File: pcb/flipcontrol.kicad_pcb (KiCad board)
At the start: 2 copper layers, 59.7 x 132.8 mm, 33 parts, among them J1 PROGRAMMING, J2 SERIAL_IN, J3 18V_POWER_IN, J4 LED_STRIP, J5 DOT_BOARD, Q1 FQP27P06, Q2 2N3904BU, Q3 FQP27P06, Q4 2N3904BU, U1 LM2576HVT-5, U2 LM1085-3.3

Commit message: Update for Kicad 7, update some components
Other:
- net class 4A trace removed
- net class Default removed

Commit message: Update PCB
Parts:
- removed J1: PROGRAMMING, Connector_PinHeader_2.54mm:PinHeader_1x04_P2.54mm_Vertical
- removed the J2 at (142.0, 80.8)
- removed MOD1: ESP32-WROOM-32, digikey-footprints:ESP32-WROOM-32D
- removed the R3 at (105.0, 68.1)
- removed the R5 at (109.8, 158.8)
- removed S2: RESET, pushbutton:1825910-6
- added C6: 100nF, Capacitor_SMD:C_0805_2012Metric, F.Cu at (21.4, 83.6)
- added C7: 10uF, Capacitor_SMD:C_0805_2012Metric, F.Cu at (21.4, 86.6)
- added C8: 100nF, Capacitor_SMD:C_0805_2012Metric, F.Cu at (21.4, 89.6)
- added C9: 10uF, Capacitor_SMD:C_0805_2012Metric, F.Cu at (21.4, 92.6)
- added D3: D, Diode_SMD:D_SOD-123, F.Cu at (11.7, 93.3)
- added D4: D, Diode_SMD:D_SOD-123, F.Cu at (11.7, 96.7)
- added F1: Polyfuse, Fuse:Fuse_1206_3216Metric, F.Cu at (26.4, 97.6)
- added J5: DOT_BOARD_3, Connector_IDC:IDC-Header_2x07_P2.54mm_Vertical, F.Cu at (96.6, 129.4)
- added Q5: MMBT3904, Package_TO_SOT_SMD:SOT-23, F.Cu at (206.1, 85.9)
- added R1: 10K, Resistor_SMD:R_0805_2012Metric, F.Cu at (16.9, 80.5)
- added R10: 5.1K, Resistor_SMD:R_0805_2012Metric, F.Cu at (16.9, 98.2)
- added R4: 2K, Resistor_SMD:R_0805_2012Metric, F.Cu at (16.9, 83.5)
- added R8: 10K, Resistor_SMD:R_0805_2012Metric, F.Cu at (210.6, 69.2)
- added R9: 5.1K, Resistor_SMD:R_0805_2012Metric, F.Cu at (16.9, 95.3)
- added U3: ESP32-S3-WROOM-1, Espressif:ESP32-S3-WROOM-1, F.Cu at (126.2, 111.0)
- added U4: CH340C, Package_SO:SOIC-16_3.9x9.9mm_P1.27mm, F.Cu at (143.6, 105.4)
- C1: value 0.1uF -> 100nF; footprint Capacitor_THT:C_Disc_D3.0mm_W1.6mm_P2.50mm -> Capacitor_SMD:C_0805_2012Metric
- C2: footprint Capacitor_THT:CP_Radial_D5.0mm_P2.50mm -> Capacitor_SMD:CP_Elec_10x10
- C3, C4: footprint Capacitor_THT:CP_Radial_D5.0mm_P2.50mm -> Capacitor_SMD:C_0805_2012Metric
- C5: value 330uF -> 220uF; footprint Capacitor_THT:CP_Radial_D5.0mm_P2.50mm -> Capacitor_SMD:CP_Elec_10x10
- D1: footprint Diode_THT:D_DO-15_P10.16mm_Horizontal -> Diode_SMD:D_SMB
- D2: value D_Schottky -> ESP_LED; footprint Diode_THT:D_DO-15_P10.16mm_Horizontal -> LED_SMD:LED_0805_2012Metric
- J2: renamed from J5; value DOT_BOARD -> DOT_BOARD_1
- J3: value 18V_POWER_IN -> DOT_BOARD_2; footprint Connector_Wire:SolderWirePad_1x02_P5.08mm_Drill1.5mm -> Connector_IDC:IDC-Header_2x07_P2.54mm_Vertical
- L1: value 220uH -> 33uH; footprint Inductor_THT:L_Radial_D8.7mm_P5.00mm_Fastron_07HCP -> Inductor_SMD:L_12x12mm_H6mm
- Q1: value FQP27P06 -> UMH3N; footprint digikey-footprints:TO-220-3 -> SamacSys_Parts:SOT65P230X110-6N
- Q2, Q4: value 2N3904BU -> AO4419; footprint digikey-footprints:TO-92-3 -> SamacSys_Parts:SOIC127P600X175-8N
- Q3: value FQP27P06 -> MMBT3904; footprint digikey-footprints:TO-220-3 -> Package_TO_SOT_SMD:SOT-23
- R2: renamed from R1; footprint Resistor_THT:R_Axial_DIN0204_L3.6mm_D1.6mm_P5.08mm_Horizontal -> Resistor_SMD:R_0805_2012Metric
- R3: renamed from R2; footprint Resistor_THT:R_Axial_DIN0204_L3.6mm_D1.6mm_P5.08mm_Horizontal -> Resistor_SMD:R_0805_2012Metric
- R5: renamed from R4; footprint Resistor_THT:R_Axial_DIN0204_L3.6mm_D1.6mm_P5.08mm_Horizontal -> Resistor_SMD:R_0805_2012Metric
- R6: value 10K -> 100R; footprint Resistor_THT:R_Axial_DIN0204_L3.6mm_D1.6mm_P5.08mm_Horizontal -> Resistor_SMD:R_0805_2012Metric
- R7: footprint Resistor_THT:R_Axial_DIN0204_L3.6mm_D1.6mm_P5.08mm_Horizontal -> Resistor_SMD:R_0805_2012Metric
- S1: value PROGRAM -> RESET; footprint pushbutton:1825910-6 -> SamacSys_Parts:FSM2JRT
- U1: value LM2576HVT-5 -> LM2596S-5; footprint Package_TO_SOT_THT:TO-220-5_Vertical -> Package_TO_SOT_SMD:TO-263-5_TabPin3
- U2: value LM1085-3.3 -> AMS1117-3.3; footprint digikey-footprints:TO-220-3 -> Package_TO_SOT_SMD:SOT-223-3_TabPin2
- moved R7 119.3 mm to (199.2, 79.5)
- moved R6 112.7 mm to (194.3, 66.0)
- moved D1 112.4 mm to (220.1, 157.9)
- moved D2 104.3 mm to (21.4, 95.6)
- moved Q4 102.9 mm to (184.4, 78.1), turned to 0 degrees
- moved C1 94.4 mm to (21.4, 80.6), turned to 0 degrees
- moved J4 93.5 mm to (188.2, 91.0)
- moved S1 89.1 mm to (36.7, 98.0)
- moved C5 82.0 mm to (224.1, 141.2)
- moved Q1 80.5 mm to (26.3, 106.6), turned to 0 degrees
- moved R5 78.8 mm to (183.4, 135.6)
- moved L1 78.4 mm to (196.9, 142.6)
- moved U1 78.1 mm to (165.5, 170.0), turned to 0 degrees
- moved C2 73.3 mm to (178.7, 154.6)
- moved J3 69.2 mm to (96.3, 99.9), turned to 0 degrees
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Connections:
- C1 pad 1: GND -> EN
- C1 pad 2: +3V3 -> GND
- D2 pad 1: +24V -> GND
- D2 pad 2: Net-(D2-Pad2) -> Net-(D2-A)
- J2 pad 10: ROW_ADVANCE -> ROW_ADVANCE_1
- J2 pad 13: Net-(J5-Pad13) -> COIL_DRIVE_OUT
- J2 pad 14: +24V -> COIL_DRIVE_OUT
- J2 pad 6: Net-(J5-Pad6) -> GND
- J2 pad 7: COL_ADVANCE -> COL_ADVANCE_1
- J2 pad 8: RESET -> RESET_1
- J2 pad 9: SET_UNSET -> SET_UNSET_1
- J3 pad 1: Net-(D2-Pad2) -> GND
- J3 pad 2: GND -> ENABLE_1
- Q1 pad 1: Net-(Q1-Pad1) -> RTS
- Q1 pad 2: COIL_DRIVE_OUT -> DTR
- Q1 pad 3: +24V -> IO0
- Q2 pad 1: GND -> +24V
- Q2 pad 2: Net-(Q2-Pad2) -> +24V
- Q2 pad 3: Net-(Q2-Pad3) -> +24V
- Q3 pad 1: Net-(Q3-Pad1) -> Net-(Q3-B)
- Q3 pad 2: LED_OUT -> GND
- Q3 pad 3: +24V -> Net-(Q3-C)
- Q4 pad 1: GND -> +24V
- Q4 pad 2: Net-(Q4-Pad2) -> +24V
- Q4 pad 3: Net-(Q4-Pad3) -> +24V
- R2 pad 1: Net-(Q2-Pad3) -> Net-(Q3-C)
- R2 pad 2: Net-(Q1-Pad1) -> Net-(Q2-G)
- R3 pad 1: Net-(Q2-Pad2) -> Net-(Q3-B)
- R5 pad 2: Net-(Q2-Pad3) -> Net-(Q3-C)
- R6 pad 1: Net-(Q4-Pad2) -> Net-(Q5-C)
- R6 pad 2: LED_IN -> Net-(Q4-G)
- R7 pad 1: +24V -> Net-(Q5-B)
- R7 pad 2: Net-(Q4-Pad3) -> LED_IN
- S1 pad 2: Net-(S1-Pad2) -> EN
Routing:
- net +5V: track 159.7 -> 0.00 mm, vias 2 -> 0
- net +24V: track 131.8 -> 0.00 mm, vias 4 -> 0
- net +3V3: track 102.9 -> 0.00 mm
- net LED_IN: track 88.2 -> 0.00 mm, vias 4 -> 0
- net COIL_DRIVE_IN: track 71.7 -> 0.00 mm, vias 2 -> 0
- net Net-(MOD1-Pad3): track 69.8 -> 0.00 mm
- net LED_OUT: track 59.1 -> 0.00 mm
- net SET_UNSET: track 53.1 -> 0.00 mm, vias 2 -> 0
- net ROW_ADVANCE: track 49.6 -> 0.00 mm, vias 2 -> 0
- net ENABLE_2: track 47.4 -> 0.00 mm
- net COL_ADVANCE: track 45.3 -> 0.00 mm, vias 2 -> 0
- net ENABLE_4: track 44.2 -> 0.00 mm
- net RESET: track 41.2 -> 0.00 mm, vias 2 -> 0
- net ENABLE_3: track 40.8 -> 0.00 mm
- net ENABLE_1: track 36.2 -> 0.00 mm
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- removed copper zone on F.Cu, net GND
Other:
- board text added: "Will Furnell 2023"
- board text added: "r2"
- board text removed: "+"
- board text removed: "-"
- board text removed: "18V IN"
- board text removed: "Note: This board has 18V, 5V and 3.3V rails!"
- board text removed: "PROGRAM"
- board text removed: "Will Furnell 2019"
- board text removed: "r1"
- board text removed: "will was here"

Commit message: Update with latest schematic and board changes
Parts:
- Q2, Q4: value AO4419 -> Si2347DS-T1-GE3; footprint SamacSys_Parts:SOIC127P600X175-8N -> SamacSys_Parts:SOT95P237X112-3N
- moved J4 106.9 mm to (117.5, 171.1), turned to 90 degrees
- moved L1 75.7 mm to (121.6, 150.1), turned to 180 degrees
- moved S1 63.8 mm to (80.5, 51.6)
- moved U3 57.0 mm to (120.3, 54.3)
- moved U1 31.6 mm to (141.0, 150.1)
- moved D2 29.8 mm to (51.2, 97.3)
- moved R1 29.8 mm to (46.7, 82.2)
- moved R10 29.8 mm to (46.7, 99.9)
- moved R4 29.8 mm to (46.7, 85.1)
- moved R9 29.8 mm to (46.7, 96.9)
- moved C1 29.8 mm to (51.2, 82.2)
- moved C6 29.8 mm to (51.2, 85.2)
- moved C7 29.8 mm to (51.2, 88.2)
- moved C8 29.8 mm to (51.2, 91.3)
- moved D3 29.8 mm to (41.5, 95.0)
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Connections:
- Q2 pad 1: +24V -> Net-(Q2-G)
- Q2 pad 3: +24V -> COIL_DRIVE_OUT
- Q4 pad 1: +24V -> Net-(Q4-G)
- Q4 pad 3: +24V -> LED_OUT
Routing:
- net COIL_DRIVE_OUT: track 86.7 -> 0.00 mm

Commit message: PCB layout
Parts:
- removed Q1: UMH3N, SamacSys_Parts:SOT65P230X110-6N
- added C10: 6.8nF, Capacitor_SMD:C_0805_2012Metric, F.Cu at (112.5, 90.4)
- added C11: 6.8nF, Capacitor_SMD:C_0805_2012Metric, F.Cu at (112.5, 93.0)
- added C12: 22nF, Capacitor_SMD:C_0805_2012Metric, F.Cu at (111.6, 108.5)
- added C13: 10nF, Capacitor_SMD:C_0805_2012Metric, F.Cu at (104.4, 82.5)
- added C14: 10nF, Capacitor_SMD:C_0805_2012Metric, F.Cu at (135.6, 97.1)
- added C15: 4.7uF, Capacitor_SMD:C_0805_2012Metric, F.Cu at (131.1, 100.4)
- added C16: 0.1uF, Capacitor_SMD:C_0805_2012Metric, F.Cu at (133.7, 100.4)
- added C17: 0.1uF, Capacitor_SMD:C_0805_2012Metric, F.Cu at (128.6, 100.4)
- added C18: 0.1uF, Capacitor_SMD:C_0805_2012Metric, F.Cu at (126.0, 100.4)
- added C19: 0.1uF, Capacitor_SMD:C_0805_2012Metric, F.Cu at (121.2, 89.4)
- added C20: 0.1uF, Capacitor_SMD:C_0805_2012Metric, F.Cu at (122.2, 93.7)
- added C21: 0.1uF, Capacitor_SMD:C_0805_2012Metric, F.Cu at (122.2, 95.8)
- added C22: 10uF/16V, Capacitor_SMD:C_0805_2012Metric, F.Cu at (137.5, 100.6)
- added C23: 10uF/16v, Capacitor_SMD:C_0805_2012Metric, F.Cu at (128.7, 84.7)
- added C24: 0.1uF, Capacitor_SMD:C_0805_2012Metric, F.Cu at (132.1, 84.7)
- added C25: 18pF, Capacitor_SMD:C_0805_2012Metric, F.Cu at (142.0, 88.2)
- added C26: 18pF, Capacitor_SMD:C_0805_2012Metric, F.Cu at (146.0, 94.5)
- added C27: 47 pF, Capacitor_SMD:C_0805_2012Metric, F.Cu at (193.6, 104.5)
- added C28: 47uF 3mΩ 16V, Capacitor_SMD:C_1210_3225Metric, F.Cu at (180.8, 92.4)
- added D5: 3V3, LED_SMD:LED_0805_2012Metric, F.Cu at (156.8, 106.3)
- added J1: PJ-202A, digikey-footprints:Barrel_Jack_5.5mmODx2.1mmID_PJ-202A, F.Cu at (208.2, 88.7)
- added J6: RJMG163118101NR, SamacSys_Parts:RJMG163118101NR, F.Cu at (104.5, 100.3)
- added J7: FTDI, Connector_PinHeader_2.54mm:PinHeader_1x06_P2.54mm_Vertical, F.Cu at (116.9, 118.6)
- added JP1: Bootloader, digikey-footprints:Jumper_Tin_P5.32mm, F.Cu at (126.2, 111.8)
- added L2: HH-1M1608-121JT, Inductor_SMD:L_0805_2012Metric, F.Cu at (141.1, 99.6)
- added R11: 33R, Resistor_SMD:R_0805_2012Metric, F.Cu at (116.9, 90.4)
- added R12: 33R, Resistor_SMD:R_0805_2012Metric, F.Cu at (116.9, 93.0)
- added R13: 33R, Resistor_SMD:R_0805_2012Metric, F.Cu at (112.5, 100.1)
- added R14: 33R, Resistor_SMD:R_0805_2012Metric, F.Cu at (112.5, 96.9)
- added R15: 49R9, Resistor_SMD:R_0805_2012Metric, F.Cu at (112.3, 104.1)
- added R16: 49R9, Resistor_SMD:R_0805_2012Metric, F.Cu at (115.9, 104.1)
- added R17: 10R, Resistor_SMD:R_0805_2012Metric, F.Cu at (104.7, 108.2)
- added R18: 49R9, Resistor_SMD:R_0805_2012Metric, F.Cu at (114.6, 86.1)
- added R19: 49R9, Resistor_SMD:R_0805_2012Metric, F.Cu at (117.1, 86.1)
- added R20: 12.4k 1%, Resistor_SMD:R_0805_2012Metric, F.Cu at (123.5, 100.3)
- added R21: 330R, Resistor_SMD:R_0805_2012Metric, F.Cu at (99.6, 108.0)
- added R22: 330R, Resistor_SMD:R_0805_2012Metric, F.Cu at (99.1, 82.5)
- added R23: 1M, Resistor_SMD:R_0805_2012Metric, F.Cu at (136.4, 92.7)
- added R25: 0.015 R, Resistor_SMD:R_0805_2012Metric, F.Cu at (157.9, 81.5)
- added R26: 10K, Resistor_SMD:R_0805_2012Metric, F.Cu at (127.8, 109.0)
- added R27: 52.3k, Resistor_SMD:R_0805_2012Metric, F.Cu at (196.1, 104.5)
- added R28: 10k, Resistor_SMD:R_0805_2012Metric, F.Cu at (198.7, 104.5)
- added R29: R_Small, Resistor_SMD:R_0805_2012Metric, F.Cu at (160.6, 101.6)
- added R30: R_Small, Resistor_SMD:R_0805_2012Metric, F.Cu at (156.8, 101.6)
- added TP1: Drive sense, TestPoint:TestPoint_Pad_D2.0mm, F.Cu at (141.0, 79.5)
- added TP2: Drive in, TestPoint:TestPoint_Pad_D2.0mm, F.Cu at (151.4, 90.7)
- added TP3: LED in, TestPoint:TestPoint_Pad_D2.0mm, F.Cu at (165.4, 87.1)
- added TP4: CS, TestPoint:TestPoint_Pad_D2.0mm, F.Cu at (128.1, 123.4)
- added TP5: SCLK, TestPoint:TestPoint_Pad_D2.0mm, F.Cu at (116.6, 123.4)
- added TP6: MISO, TestPoint:TestPoint_Pad_D2.0mm, F.Cu at (124.3, 123.4)
- added TP7: MOSI, TestPoint:TestPoint_Pad_D2.0mm, F.Cu at (120.4, 123.4)
- added U5: W5500, Package_QFP:LQFP-48_7x7mm_P0.5mm, F.Cu at (129.6, 92.6)
- added USB1: HRO-TYPE-C-31-M-12, Connector_USB:USB_C_Receptacle_HRO_TYPE-C-31-M-12, F.Cu at (174.6, 123.4)
- added Y1: Crystal_GND24, Crystal:Crystal_SMD_Abracon_ABM8G-4Pin_3.2x2.5mm, F.Cu at (142.4, 92.4)
- C2: value 100uF -> 10uF 2.8mΩ 35V; footprint Capacitor_SMD:CP_Elec_10x10 -> Capacitor_SMD:C_0805_2012Metric
- C5: value 220uF -> 100nF 30mΩ 50V; footprint Capacitor_SMD:CP_Elec_10x10 -> Capacitor_SMD:C_0805_2012Metric
- C9: value 10uF -> 100 nF 1mΩ 10V
- D1: value D_Schottky -> 5V; footprint Diode_SMD:D_SMB -> LED_SMD:LED_0805_2012Metric
- L1: value 33uH -> IHLP4040DZER6R8M01; footprint Inductor_SMD:L_12x12mm_H6mm -> Inductor_SMD:L_Vishay_IHLP-4040
- U1: value LM2596S-5 -> TPS563300; footprint Package_TO_SOT_SMD:TO-263-5_TabPin3 -> Package_TO_SOT_SMD:SOT-583-8
- U4: value CH340C -> NCS214; footprint Package_SO:SOIC-16_3.9x9.9mm_P1.27mm -> Package_TO_SOT_SMD:SOT-363_SC-70-6_Handsoldering
- moved D3 160.3 mm to (201.7, 91.3), turned to 90 degrees
- moved C9 145.8 mm to (196.8, 101.6)
- moved D4 140.3 mm to (181.5, 106.0), turned to -90 degrees
- moved R10 130.3 mm to (176.3, 113.6), turned to -90 degrees
- moved R9 126.4 mm to (172.0, 113.6), turned to -90 degrees
- moved F1 125.5 mm to (180.9, 113.0), turned to 90 degrees
- moved J4 117.2 mm to (193.4, 81.8), turned to -90 degrees
- moved R1 114.0 mm to (154.4, 119.6), turned to 180 degrees
- moved H2 111.9 mm to (209.4, 75.4), turned to -90 degrees
- moved S1 110.0 mm to (163.9, 123.4)
- moved C6 109.6 mm to (154.4, 122.2), turned to 180 degrees
- moved C7 109.5 mm to (154.4, 124.7)
- moved C1 108.9 mm to (154.4, 117.1)
- moved C8 96.7 mm to (147.4, 82.1), turned to 180 degrees
- moved H1 93.4 mm to (209.7, 115.6), turned to -90 degrees
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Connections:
- C2 pad 1: +24V -> +18V
- C5 pad 1: +5V -> +18V
- C9 pad 1: GND -> Net-(U1-SW)
- C9 pad 2: +3V3 -> Net-(U1-VBST)
- D1 pad 1: Net-(D1-K) -> GND
- D1 pad 2: GND -> Net-(D1-A)
- D3 pad 1: +24V -> +18V
- F1 pad 1: Net-(D4-A) -> USB_VBUS
- F1 pad 2: Net-(F1-Pad2) -> Net-(D4-A)
- L1 pad 1: Net-(D1-K) -> Net-(U1-SW)
- Q2 pad 2: +24V -> +18V
- Q2 pad 3: COIL_DRIVE_OUT -> Net-(Q2-D)
- Q4 pad 2: +24V -> +18V
- R5 pad 1: +24V -> +18V
- R8 pad 1: +24V -> +18V
- U1 pad 1: +24V -> unconnected-(U1-NC-Pad1)
- U1 pad 2: Net-(D1-K) -> unconnected-(U1-EN-Pad2)
- U1 pad 3: GND -> +18V
- U1 pad 4: +5V -> GND
- U1 pad 5: GND -> Net-(U1-SW)
- U3 pad 10: ROW_ADVANCE_2 -> SET_UNSET_2
- U3 pad 11: COL_ADVANCE_2 -> ROW_ADVANCE_2
- U3 pad 12: COL_ADVANCE_1 -> COL_ADVANCE_2
- U3 pad 13: unconnected-(U3-GPIO19/U1RTS/ADC2_CH8/CLK_OUT2/USB_D--Pad13) -> USB_DN
- U3 pad 14: unconnected-(U3-GPIO20/U1CTS/ADC2_CH9/CLK_OUT1/USB_D+-Pad14) -> USB_DP
- U3 pad 15: unconnected-(U3-GPIO3/TOUCH3/ADC1_CH2-Pad15) -> COIL_DRIVE_SENSE
- U3 pad 16: COL_ADVANCE_3 -> unconnected-(U3-GPIO46-Pad16)
- U3 pad 17: RESET_1 -> RESET_2
- U3 pad 22: SET_UNSET_2 -> RESET_3
- U3 pad 23: RESET_2 -> COL_ADVANCE_3
- U3 pad 24: RESET_3 -> ROW_ADVANCE_3
- U3 pad 25: ESP_LED -> SET_UNSET_3
- U3 pad 26: ROW_ADVANCE_3 -> unconnected-(U3-GPIO45-Pad26)
- U3 pad 28: unconnected-(U3-SPIIO6/GPIO35/FSPID/SUBSPID-Pad28) -> MOSI
- U3 pad 29: unconnected-(U3-SPIIO7/GPIO36/FSPICLK/SUBSPICLK-Pad29) -> SCLK
- U3 pad 30: unconnected-(U3-SPIDQS/GPIO37/FSPIQ/SUBSPIQ-Pad30) -> MISO
- U3 pad 31: SET_UNSET_3 -> ESP_LED
- U3 pad 34: unconnected-(U3-MTDI/GPIO41/CLK_OUT1-Pad34) -> ETH_RST
- U3 pad 35: unconnected-(U3-MTMS/GPIO42-Pad35) -> CS
- U3 pad 38: unconnected-(U3-GPIO2/TOUCH2/ADC1_CH1-Pad38) -> COIL_DRIVE_IN
- U3 pad 39: unconnected-(U3-GPIO1/TOUCH1/ADC1_CH0-Pad39) -> LED_IN
- U3 pad 4: LED_IN -> RESET_1
- U3 pad 5: COIL_DRIVE_IN -> COL_ADVANCE_1
- U3 pad 6: SET_UNSET_1 -> ROW_ADVANCE_1
- U3 pad 7: ROW_ADVANCE_1 -> SET_UNSET_1
- U4 pad 2: ESP_RXD -> GND
- U4 pad 3: ESP_TXD -> +3V3
- U4 pad 4: +3V3 -> Net-(Q2-D)
- U4 pad 5: Net-(U4-UD+) -> COIL_DRIVE_OUT
- U4 pad 6: Net-(U4-UD-) -> COIL_DRIVE_SENSE
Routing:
- net +3V3: track 0.00 -> 235.3 mm, vias 0 -> 4
- net +5V: track 0.00 -> 185.3 mm, vias 0 -> 3
- net ENABLE_2: track 0.00 -> 122.9 mm, vias 0 -> 2
- net ENABLE_4: track 0.00 -> 122.2 mm, vias 0 -> 1
- net ENABLE_3: track 0.00 -> 120.0 mm, vias 0 -> 4
- net ENABLE_1: track 0.00 -> 115.0 mm, vias 0 -> 2
- net +3.3VA: track 0.00 -> 112.2 mm, vias 0 -> 7
- net COIL_DRIVE_OUT: track 0.00 -> 87.9 mm, vias 0 -> 1
- net +18V: track 0.00 -> 79.9 mm, vias 0 -> 2
- net COL_ADVANCE_1: track 0.00 -> 64.5 mm, vias 0 -> 1
- net LED_IN: track 0.00 -> 63.5 mm, vias 0 -> 2
- net RESET_1: track 0.00 -> 63.3 mm, vias 0 -> 1
- net COL_ADVANCE_3: track 0.00 -> 63.0 mm, vias 0 -> 1
- net SET_UNSET_1: track 0.00 -> 60.9 mm, vias 0 -> 1
- net ROW_ADVANCE_1: track 0.00 -> 59.7 mm, vias 0 -> 1
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- added copper zone on F.Cu, net GND
- added copper zone on In1.Cu, net GND
- added copper zone on In2.Cu, net GND
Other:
- board size 59.7 x 132.8 mm -> 133.4 x 61.7 mm
- copper layers 2 -> 4
- rule pad_to_mask_clearance: 0.051 -> 0
- rule solder_mask_min_width: 0.25 -> 0.13
- board text added: "Flipdot Controller for Hanover Displays"
- board text added: "Reset"
- board text added: "Revision 1.0"
- board text added: "https://github.com/willfurnell/esp32-flipdot-controller"
- board text removed: "Flipdot Controller"
- board text removed: "RESET"
- board text removed: "Will Furnell 2023"
- board text removed: "based on a design by damow"
- board text removed: "for Hanover Displays"
- board text removed: "r2"
- board text removed: "willfurnell.com"

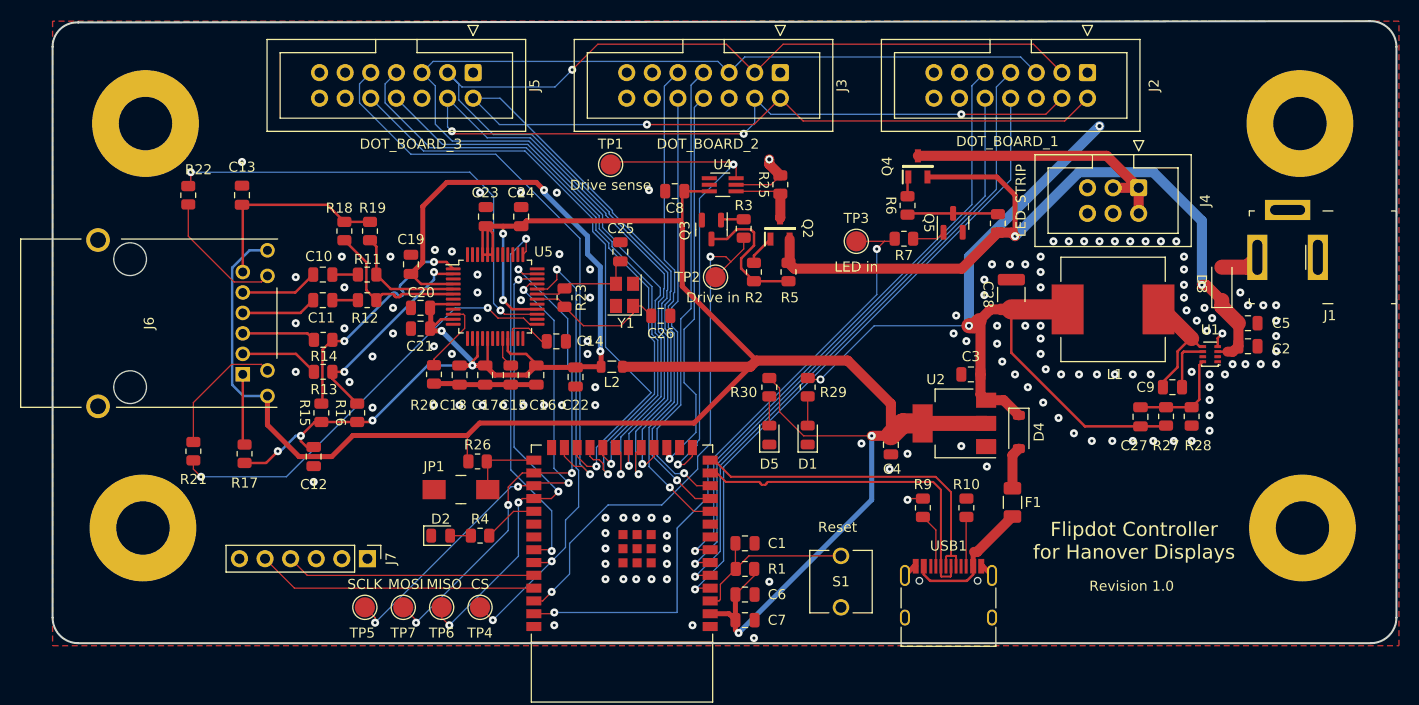
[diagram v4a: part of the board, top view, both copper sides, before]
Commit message: Fix board being ever so slightly off square
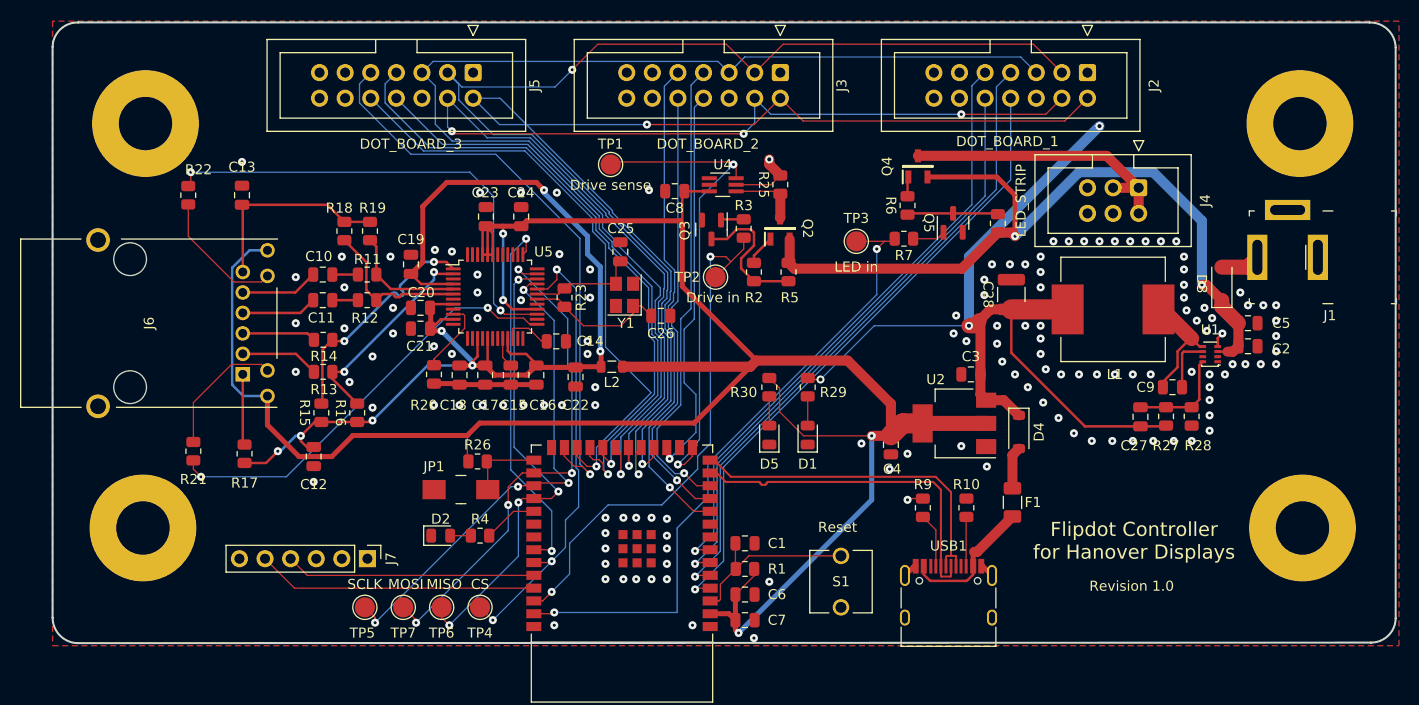
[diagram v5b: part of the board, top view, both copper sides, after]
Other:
- board size 133.4 x 61.7 mm -> 133.3 x 61.6 mm
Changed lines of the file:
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@@
   (gr_line (start 85.65 124.46) (end 85.65 67.818)
     (stroke (width 0.2) (type default)) (layer "Edge.Cuts"))
-  (gr_arc (start 219 124.46) (mid 218.256051 126.256051) (end 216.46 127)
+  (gr_arc (start 218.924558 124.531837) (mid 218.191992 126.247823) (end 216.460605 126.943206)
     (stroke (width 0.2) (type default)) (layer "Edge.Cuts"))
-  (gr_arc (start 85.65 67.818) (mid 86.402196 66.067486) (end 88.189825 65.408335)
+  (gr_arc (start 85.65 67.818) (mid 86.420855 66.087153) (end 88.189825 65.408335)
     (stroke (width 0.2) (type default)) (layer "Edge.Cuts"))
   (gr_arc (start 88.19 127) (mid 86.393949 126.256051) (end 85.65 124.46)
     (stroke (width 0.2) (type default)) (layer "Edge.Cuts"))
-  (gr_line (start 216.46 127) (end 88.19 127)
+  (gr_line (start 216.460605 126.943206) (end 88.19 127)
     (stroke (width 0.2) (type default)) (layer "Edge.Cuts"))
-  (gr_arc (start 216.333 65.278001) (mid 218.213449 65.987495) (end 219.002316 67.836051)
+  (gr_arc (start 216.333 65.408336) (mid 218.14245 66.111717) (end 218.924559 67.888557)
     (stroke (width 0.2) (type default)) (layer "Edge.Cuts"))
-  (gr_line (start 219.002316 67.836051) (end 219 124.46)
+  (gr_line (start 218.924559 67.888557) (end 218.924559 124.531837)
     (stroke (width 0.2) (type default)) (layer "Edge.Cuts"))
-  (gr_line (start 88.189825 65.408335) (end 216.333 65.278)
+  (gr_line (start 88.189825 65.408335) (end 216.333 65.408335)
     (stroke (width 0.2) (type default)) (layer "Edge.Cuts"))
   (gr_text "https://github.com/willfurnell/esp32-flipdot-controller" (at 212.65 109.22) (layer "B.SilkS")
